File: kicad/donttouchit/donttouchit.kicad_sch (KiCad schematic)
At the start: 52 parts, among them J1 Conn_01x02_Female, J10 Conn_01x04_Male, J2 Conn_01x02_Female, J3 Conn_01x02_Female, J4 Conn_01x02_Female, J5 Conn_01x02_Female, J6 Conn_01x02_Female, J7 Conn_01x02_Female, J8 Conn_01x02_Female, J9 Conn_01x02_Female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

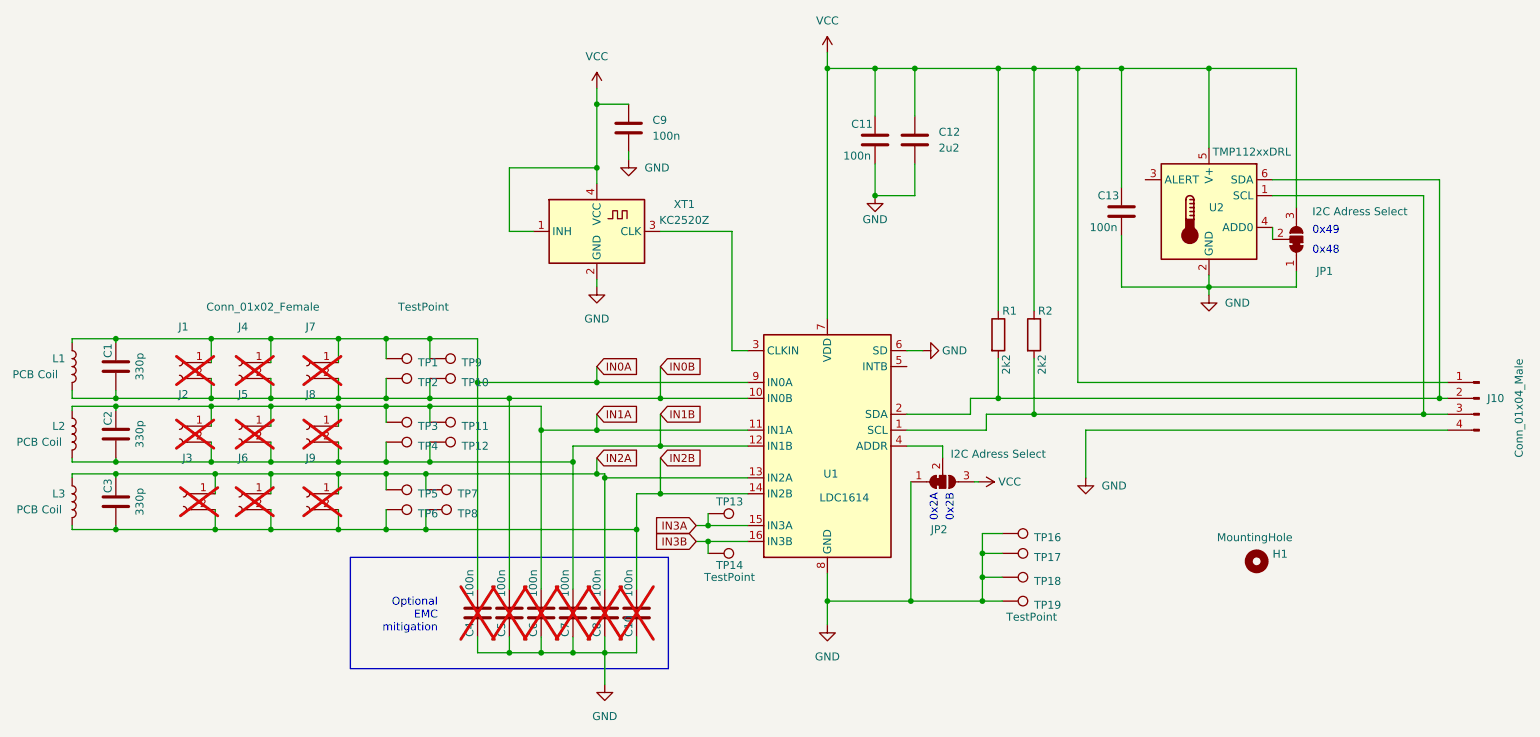
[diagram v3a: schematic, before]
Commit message: ESD capacitor values corrected / Tempsensor name updated
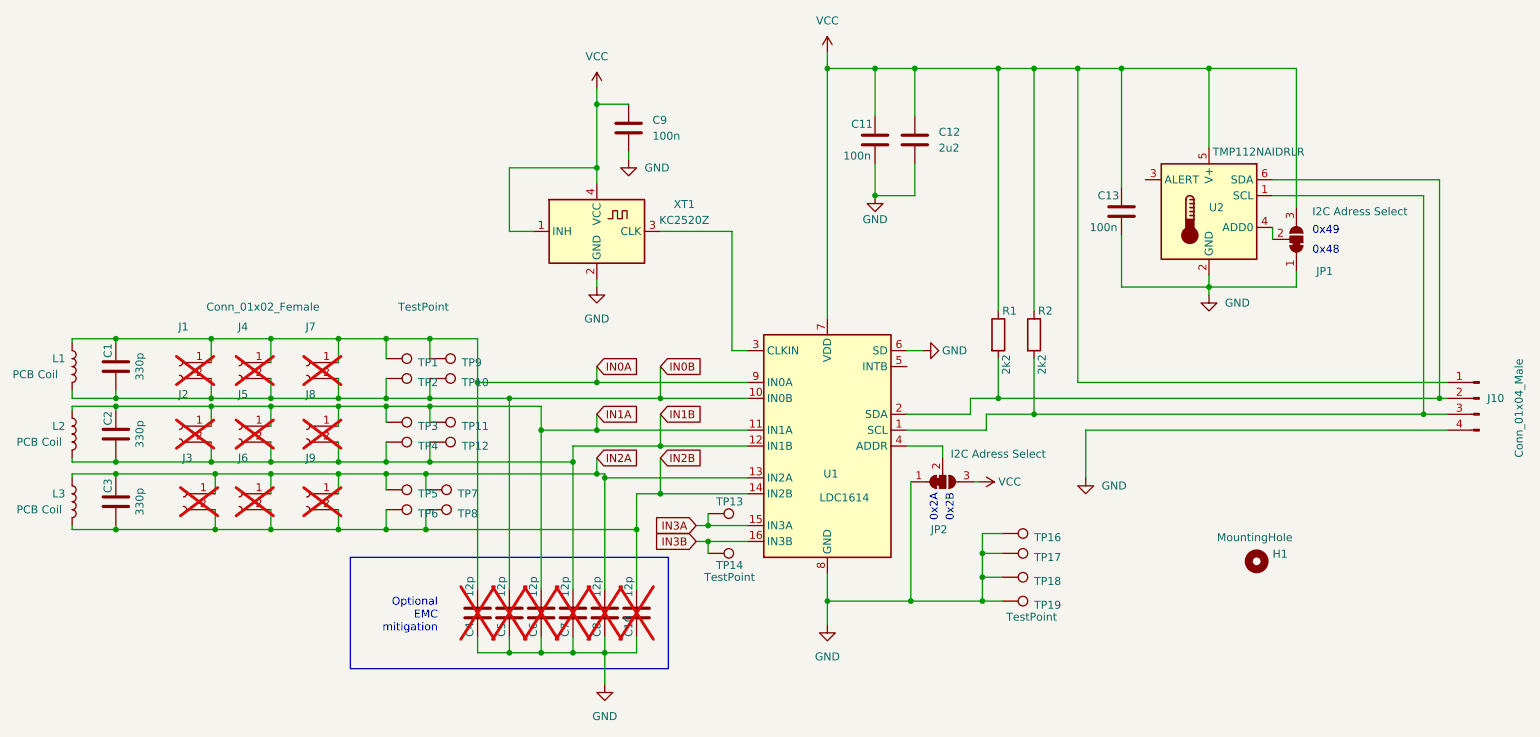
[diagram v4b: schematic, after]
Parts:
- C10, C4, C5, C6, C7, C8: value 100n -> 12p
- U2: value TMP112xxDRL -> TMP112NAIDRLR
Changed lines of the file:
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@@
       (effects (font (size 1.27 1.27)) (justify left))
     )
-    (property "Value" "100n" (at 134.62 135.255 90)
+    (property "Value" "12p" (at 134.62 135.255 90)
       (effects (font (size 1.27 1.27)) (justify left))
     )
@@
       (effects (font (size 1.27 1.27)) (justify left))
     )
-    (property "Value" "100n" (at 124.46 135.255 90)
+    (property "Value" "12p" (at 124.46 135.255 90)
       (effects (font (size 1.27 1.27)) (justify left))
     )
@@
       (effects (font (size 1.27 1.27)) (justify left))
     )
-    (property "Value" "100n" (at 114.3 135.255 90)
+    (property "Value" "12p" (at 114.3 135.255 90)
       (effects (font (size 1.27 1.27)) (justify left))
     )
@@
       (effects (font (size 1.27 1.27)) (justify left))
     )
-    (property "Value" "100n" (at 129.54 135.255 90)
+    (property "Value" "12p" (at 129.54 135.255 90)
       (effects (font (size 1.27 1.27)) (justify left))
     )
@@
       (effects (font (size 1.27 1.27)) (justify left))
     )
-    (property "Value" "100n" (at 119.38 135.255 90)
+    (property "Value" "12p" (at 119.38 135.255 90)
       (effects (font (size 1.27 1.27)) (justify left))
     )
@@
       (effects (font (size 1.27 1.27)) (justify left))
     )
-    (property "Value" "100n" (at 139.7 135.255 90)
+    (property "Value" "12p" (at 139.7 135.255 90)
       (effects (font (size 1.27 1.27)) (justify left))
     )
@@
       (effects (font (size 1.27 1.27)) (justify right))
     )
-    (property "Value" "TMP112xxDRL" (at 232.9941 64.135 0)
+    (property "Value" "TMP112NAIDRLR" (at 232.9941 64.135 0)
       (effects (font (size 1.27 1.27)) (justify right))
     )
